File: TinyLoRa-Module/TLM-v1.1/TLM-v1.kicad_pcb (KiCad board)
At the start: 4 copper layers, 14 x 16.5 mm, 54 parts, among them U1 TLM01, U2 ATSAMR34J18B, U3 SKY13373-460LF, Y1 ABS05-32.768KHZ-9-T

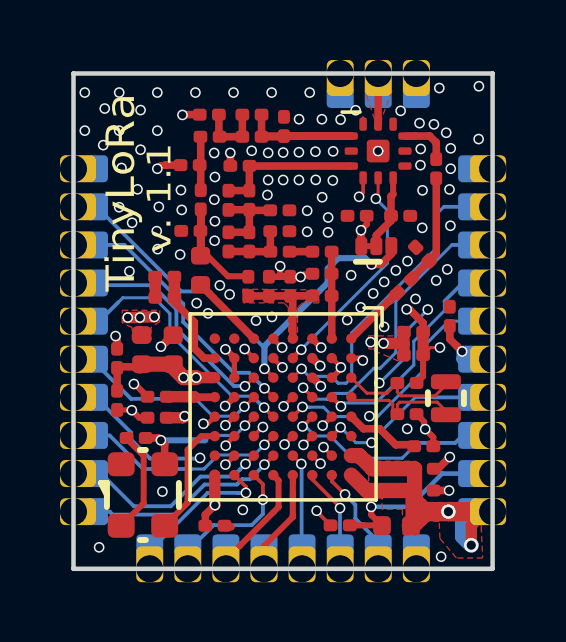
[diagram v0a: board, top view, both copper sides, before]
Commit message: BOMs added
BOMs for TinyLoRa and its breakout added
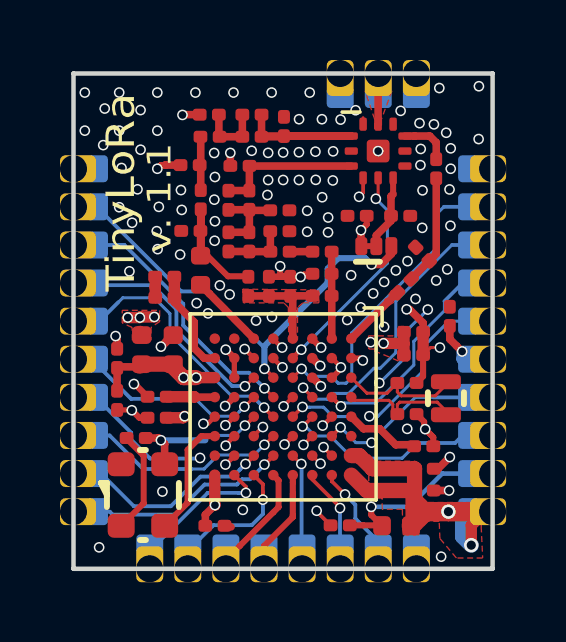
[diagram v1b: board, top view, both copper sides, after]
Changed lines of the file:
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@@
     (user_trace_width 0.635)
     (trace_clearance 0.1016)
-    (zone_clearance 0.133)
+    (zone_clearance 0.2)
     (zone_45_only no)
     (trace_min 0.1016)
@@
     (visible_elements 7FFFFF7F)
     (pcbplotparams
-      (layerselection 0x010fc_ffffffff)
+      (layerselection 0x210fc_ffffffff)
       (usegerberextensions true)
       (usegerberattributes false)
@@
   (segment (start 134.646 82.498173) (end 134.359019 82.211192) (width 0.2032) (layer Top.RF) (net 2) (status 10))
   (segment (start 134.646 82.5125) (end 134.646 82.498173) (width 0.2032) (layer Top.RF) (net 2) (status 30))
-  (via (at 134.35 82.22) (size 0.3556) (drill 0.254) (layers Top.RF Bottom.LF) (net 2))
+  (via (at 134.36 82.23) (size 0.3556) (drill 0.254) (layers Top.RF Bottom.LF) (net 2))
   (via (at 136.24 82.16) (size 0.3556) (drill 0.254) (layers Top.RF Bottom.LF) (net 2))
   (via (at 136.25 82.82) (size 0.3556) (drill 0.254) (layers Top.RF Bottom.LF) (net 2))
@@
   (via (at 137.53 83.45021) (size 0.3556) (drill 0.254) (layers Top.RF Bottom.LF) (net 20))
   (segment (start 137.619758 83.4) (end 137.557886 83.461872) (width 0.254) (layer In2.PWR) (net 20))
-  (segment (start 138.71 83.4) (end 137.619758 83.4) (width 0.254) (layer In2.PWR) (net 20))
-  (segment (start 139.307458 82.802542) (end 138.71 83.4) (width 0.254) (layer In2.PWR) (net 20))
-  (segment (start 139.615098 82.802542) (end 139.307458 82.802542) (width 0.254) (layer In2.PWR) (net 20))
+  (segment (start 138.78 83.4) (end 137.619758 83.4) (width 0.254) (layer In2.PWR) (net 20))
+  (segment (start 139.377458 82.802542) (end 138.78 83.4) (width 0.254) (layer In2.PWR) (net 20))
+  (segment (start 139.615098 82.802542) (end 139.377458 82.802542) (width 0.254) (layer In2.PWR) (net 20))
   (via (at 135 84.76) (size 0.3556) (drill 0.254) (layers Top.RF Bottom.LF) (net 21))
   (segment (start 135.296 84.474073) (end 134.985442 84.784631) (width 0.127) (layer Top.RF) (net 21) (status 10))
@@
   (segment (start 130.93 80.5) (end 130.78 80.65) (width 0.1016) (layer Bottom.LF) (net 32))
   (segment (start 131.97 80.5) (end 130.93 80.5) (width 0.1016) (layer Bottom.LF) (net 32))
-  (segment (start 134.57 83.78) (end 132.5 81.71) (width 0.1016) (layer Bottom.LF) (net 32))
+  (segment (start 135.25 83.78) (end 134.56 83.78) (width 0.1016) (layer Bottom.LF) (net 32))
   (segment (start 132.5 81.03) (end 131.97 80.5) (width 0.1016) (layer Bottom.LF) (net 32))
-  (segment (start 132.5 81.71) (end 132.5 81.03) (width 0.1016) (layer Bottom.LF) (net 32))
-  (segment (start 135.25 83.78) (end 134.57 83.78) (width 0.1016) (layer Bottom.LF) (net 32))
+  (segment (start 132.5 81.72) (end 132.5 81.03) (width 0.1016) (layer Bottom.LF) (net 32))
+  (segment (start 134.56 83.78) (end 132.5 81.72) (width 0.1016) (layer Bottom.LF) (net 32))
   (segment (start 135.27 83.8) (end 135.25 83.78) (width 0.1016) (layer Bottom.LF) (net 32))
   (segment (start 137.896 83.8125) (end 137.882121 83.8125) (width 0.127) (layer Top.RF) (net 33) (status 30))
@@
   (segment (start 135.489611 83.356111) (end 135.66741 83.53391) (width 0.127) (layer Bottom.LF) (net 35))
   (segment (start 135.1335 83) (end 135.489611 83.356111) (width 0.127) (layer Bottom.LF) (net 35))
-  (segment (start 132.944521 81.311425) (end 134.633096 83) (width 0.127) (layer Bottom.LF) (net 35))
-  (segment (start 134.633096 83) (end 135.1335 83) (width 0.127) (layer Bottom.LF) (net 35))
-  (segment (start 132.944521 80.704521) (end 132.944521 81.311425) (width 0.127) (layer Bottom.LF) (net 35))
+  (segment (start 134.52 83) (end 135.1335 83) (width 0.127) (layer Bottom.LF) (net 35))
+  (segment (start 132.944521 81.424521) (end 134.52 83) (width 0.127) (layer Bottom.LF) (net 35))
+  (segment (start 132.944521 80.704521) (end 132.944521 81.424521) (width 0.127) (layer Bottom.LF) (net 35))
   (segment (start 130.98 78.74) (end 132.944521 80.704521) (width 0.127) (layer Bottom.LF) (net 35))
   (segment (start 136.596 85.7625) (end 136.596 85.776694) (width 0.1016) (layer Top.RF) (net 36) (status 30))
@@
   (via (at 135.002126 83.44979) (size 0.3556) (drill 0.254) (layers Top.RF Bottom.LF) (net 45))
   (segment (start 129.956 80.08) (end 129.886 80.01) (width 0.127) (layer Bottom.LF) (net 45))
+  (segment (start 132.71591 81.58591) (end 132.71591 80.88591) (width 0.127) (layer Bottom.LF) (net 45))
   (segment (start 132.71591 80.88591) (end 131.91 80.08) (width 0.127) (layer Bottom.LF) (net 45))
-  (segment (start 132.71591 81.52591) (end 132.71591 80.88591) (width 0.127) (layer Bottom.LF) (net 45))
-  (segment (start 134.630887 83.440887) (end 132.71591 81.52591) (width 0.127) (layer Bottom.LF) (net 45))
   (segment (start 131.91 80.08) (end 129.956 80.08) (width 0.127) (layer Bottom.LF) (net 45))
-  (segment (start 135.002126 83.440887) (end 134.630887 83.440887) (width 0.127) (layer Bottom.LF) (net 45))
+  (segment (start 134.570887 83.440887) (end 132.71591 81.58591) (width 0.127) (layer Bottom.LF) (net 45))
+  (segment (start 135.002126 83.440887) (end 134.570887 83.440887) (width 0.127) (layer Bottom.LF) (net 45))
   (segment (start 135.946 83.1625) (end 135.946 83.177499) (width 0.1016) (layer Top.RF) (net 46) (status 30))
   (segment (start 135.946 83.1625) (end 135.946 83.149795) (width 0.127) (layer Top.RF) (net 46) (status 30))
@@
   )
   (zone (net 2) (net_name GND) (layer Bottom.LF) (hatch full 0.508)
-    (connect_pads yes (clearance 0.175))
+    (connect_pads yes (clearance 0.2))
     (min_thickness 0.2)
     (fill yes (arc_segments 32) (thermal_gap 0.3) (thermal_bridge_width 0.3) (smoothing chamfer))
@@
   )
   (zone (net 2) (net_name GND) (layer Top.RF) (hatch full 0.508)
-    (connect_pads yes (clearance 0.133))
+    (connect_pads yes (clearance 0.15))
     (min_thickness 0.2)
     (fill yes (arc_segments 32) (thermal_gap 0.3) (thermal_bridge_width 0.3) (smoothing chamfer))
@@
   )
   (zone (net 2) (net_name GND) (layer In2.PWR) (hatch full 0.508)
-    (connect_pads (clearance 0.175))
+    (connect_pads (clearance 0.2))
     (min_thickness 0.2)
     (fill yes (arc_segments 32) (thermal_gap 0.3) (thermal_bridge_width 0.3) (smoothing chamfer))
